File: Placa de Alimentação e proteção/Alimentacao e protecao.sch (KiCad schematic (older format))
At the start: 20 parts, among them J1 PinoCheckBateriaVcc, J2 PinoCheckBateriaGND, J3 8.4V_PlacaCentral, J4 GND_PlacaCentral, Q1 BC548, Q2 BC548, SW1 SW_ON/OFF

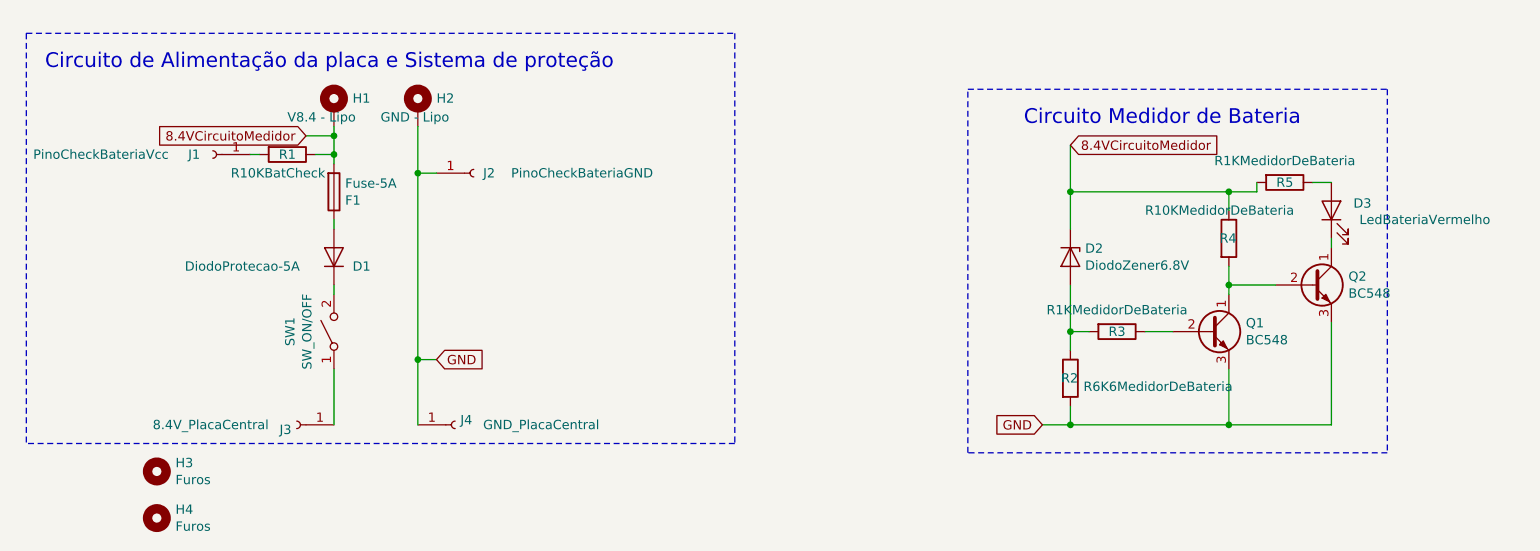
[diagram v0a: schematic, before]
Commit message: Acertos finais para documentação
Foram organizados e preparados para serem folhas em baixo de um um folha hierárquica maior, os projetos das placa de alimentação e das placas de encoder.
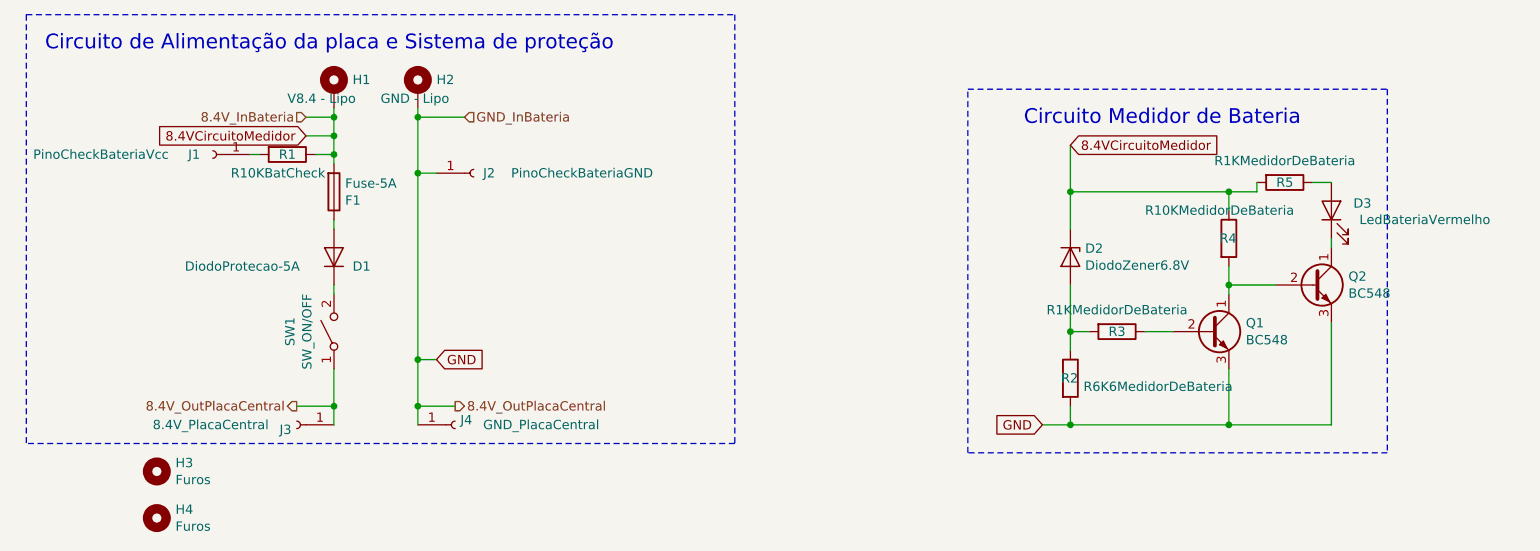
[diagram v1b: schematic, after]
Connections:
- net GND: now also J3.1 (Pin_1), SW1.1 (A)
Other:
- moved on the sheet: H1, H2
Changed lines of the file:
@@
 EESchema Schematic File Version 4
-LIBS:Alimentacao e protecao-cache
-EELAYER 29 0
+EELAYER 30 0
 EELAYER END
 $Descr A4 11693 8268
@@
 L Mechanical:MountingHole_Pad H1
 U 1 1 5D0BE091
-P 2850 1700
-F 0 "H1" H 2950 1751 50  0000 L CNN
-F 1 "V8.4 - Lipo" H 2600 1650 50  0000 L CNN
-F 2 "Connector_Wire:SolderWirePad_1x01_Drill1.5mm" H 2850 1700 50  0001 C CNN
-F 3 "~" H 2850 1700 50  0001 C CNN
-	1    2850 1700
+P 2850 1600
+F 0 "H1" H 2950 1651 50  0000 L CNN
+F 1 "V8.4 - Lipo" H 2600 1550 50  0000 L CNN
+F 2 "Connector_Wire:SolderWirePad_1x01_Drill1.5mm" H 2850 1600 50  0001 C CNN
+F 3 "~" H 2850 1600 50  0001 C CNN
+	1    2850 1600
 	1    0    0    -1
 $EndComp
@@
 L Mechanical:MountingHole_Pad H2
 U 1 1 5D0BE14B
-P 3300 1700
-F 0 "H2" H 3400 1751 50  0000 L CNN
-F 1 "GND - Lipo" H 3100 1650 50  0000 L CNN
-F 2 "Connector_Wire:SolderWirePad_1x01_Drill1.5mm" H 3300 1700 50  0001 C CNN
-F 3 "~" H 3300 1700 50  0001 C CNN
-	1    3300 1700
+P 3300 1600
+F 0 "H2" H 3400 1651 50  0000 L CNN
+F 1 "GND - Lipo" H 3100 1550 50  0000 L CNN
+F 2 "Connector_Wire:SolderWirePad_1x01_Drill1.5mm" H 3300 1600 50  0001 C CNN
+F 3 "~" H 3300 1600 50  0001 C CNN
+	1    3300 1600
 	1    0    0    -1
 $EndComp
@@
 	3400 2050 3300 2050
 Connection ~ 3300 2050
-Wire Wire Line
-	3300 2050 3300 1800
-Text Notes 1300 1500 0    79   ~ 0
+Text Notes 1300 1400 0    79   ~ 0
 Circuito de Alimentação da placa e Sistema de proteção
 Wire Notes Line
-	1200 1300 5000 1300
+	1200 1200 5000 1200
 Wire Notes Line
 	5000 3500 1200 3500
@@
 	2750 1950 2850 1950
 Wire Wire Line
-	2850 1800 2850 1850
-Wire Wire Line
 	2850 1950 2850 2000
 Connection ~ 2850 1950
@@
 Wire Wire Line
 	6800 1900 6800 2150
-Wire Notes Line
-	5000 1300 5000 3500
-Wire Notes Line
-	1200 1300 1200 3500
-Wire Wire Line
-	2850 3100 2850 3400
-Wire Wire Line
-	3300 3400 3300 3050
+Wire Wire Line
+	2850 3100 2850 3300
+Wire Wire Line
+	3300 3400 3300 3300
 Connection ~ 3300 3050
 Wire Wire Line
@@
 	6650 3400 6800 3400
 Connection ~ 6800 3400
+Text HLabel 2650 3300 0    50   Output ~ 0
+8.4V_OutPlacaCentral
+Text HLabel 3500 3300 2    50   Output ~ 0
+8.4V_OutPlacaCentral
+Text HLabel 2700 1750 0    50   Input ~ 0
+8.4V_InBateria
+Text HLabel 3550 1750 2    50   Input ~ 0
+GND_InBateria
+Wire Notes Line
+	1200 1200 1200 3500
+Wire Notes Line
+	5000 1200 5000 3500
+Wire Wire Line
+	2700 1750 2850 1750
+Wire Wire Line
+	2850 1750 2850 1700
+Wire Wire Line
+	2850 1750 2850 1850
+Connection ~ 2850 1750
+Wire Wire Line
+	3300 1700 3300 1750
+Wire Wire Line
+	3300 1750 3550 1750
+Connection ~ 3300 1750
+Wire Wire Line
+	3300 1750 3300 2050
+Wire Wire Line
+	2650 3300 2850 3300
+Connection ~ 2850 3300
+Wire Wire Line
+	2850 3300 2850 3400
+Wire Wire Line
+	3500 3300 3300 3300
+Connection ~ 3300 3300
+Wire Wire Line
+	3300 3300 3300 3050
 $EndSCHEMATC

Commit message: Ajuste final
Acertado a placa central, verificado conflitos de etiquetas hierárquicas, ligados os projeto um no outro, ajustado o projeto principal e linkado todos as placas ao projeto principal.
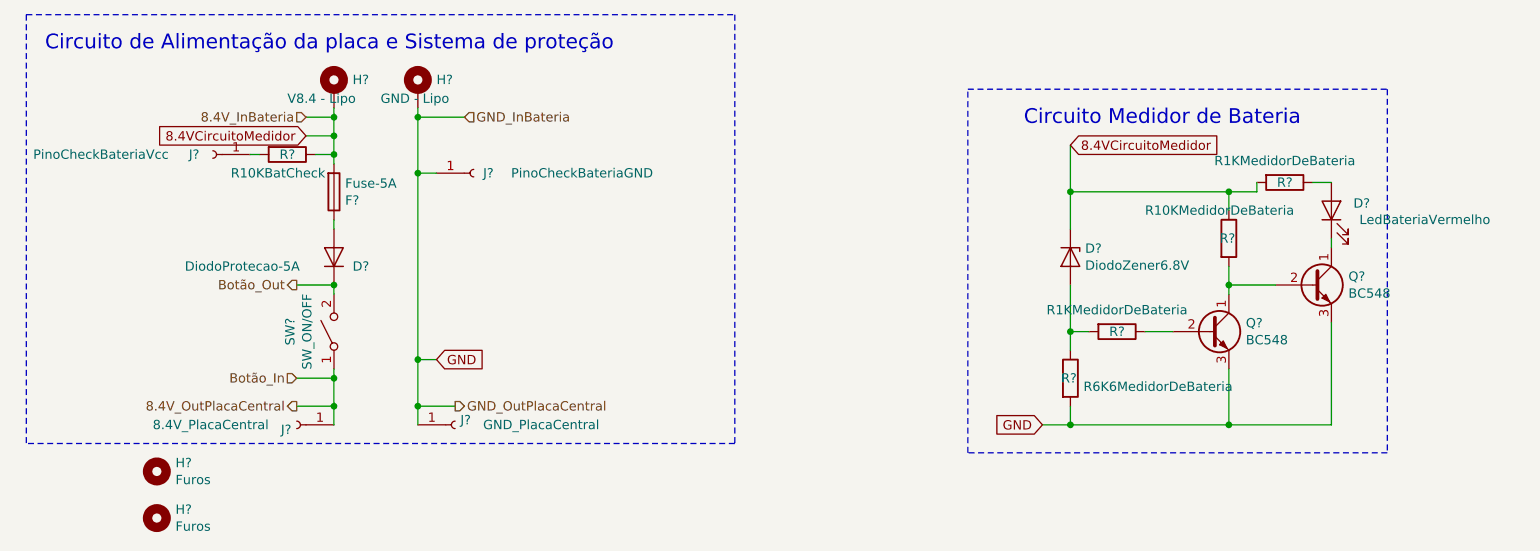
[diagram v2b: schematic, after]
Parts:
- renumbered D1 to D?, D2 to D?, D3 to D?, F1 to F?, H1 to H?, H2 to H?, H3 to H?, H4 to H?, J2 to J?, J1 to J?, J3 to J?, J4 to J?, Q1 to Q?, Q2 to Q?, R1 to R?, R3 to R?, R2 to R?, R4 to R?, R5 to R?, SW1 to SW?
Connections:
- net GND: no longer J?.1 (Pin_1), SW?.1 (A)
- net Botão_Out: now reaches D?.1 (K), SW?.2 (B)
- new net 8.4V_OutPlacaCentral: J?.1 (Pin_1), SW?.1 (A)
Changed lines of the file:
@@
 $Descr A4 11693 8268
 encoding utf-8
-Sheet 1 1
+Sheet 2 7
 Title ""
 Date ""
@@
 $EndDescr
 $Comp
-L Switch:SW_SPST SW1
+L Switch:SW_SPST SW?
 U 1 1 5D0BCA30
 P 2850 2900
-F 0 "SW1" H 2850 3135 50  0000 C CNN
+F 0 "SW?" H 2850 3135 50  0000 C CNN
 F 1 "SW_ON/OFF" H 2850 3044 50  0000 C CNN
 F 2 "CUSTOM_Placa_central_v01:Solder_Pad_Custom" H 2850 2900 50  0001 C CNN
@@
 $EndComp
 $Comp
-L Mechanical:MountingHole_Pad H1
+L Mechanical:MountingHole_Pad H?
 U 1 1 5D0BE091
 P 2850 1600
-F 0 "H1" H 2950 1651 50  0000 L CNN
+F 0 "H?" H 2950 1651 50  0000 L CNN
 F 1 "V8.4 - Lipo" H 2600 1550 50  0000 L CNN
 F 2 "Connector_Wire:SolderWirePad_1x01_Drill1.5mm" H 2850 1600 50  0001 C CNN
@@
 $EndComp
 $Comp
-L Mechanical:MountingHole_Pad H2
+L Mechanical:MountingHole_Pad H?
 U 1 1 5D0BE14B
 P 3300 1600
-F 0 "H2" H 3400 1651 50  0000 L CNN
+F 0 "H?" H 3400 1651 50  0000 L CNN
 F 1 "GND - Lipo" H 3100 1550 50  0000 L CNN
 F 2 "Connector_Wire:SolderWirePad_1x01_Drill1.5mm" H 3300 1600 50  0001 C CNN
@@
 $EndComp
 $Comp
-L Connector:Conn_01x01_Female J2
+L Connector:Conn_01x01_Female J?
 U 1 1 5D152CB0
 P 3600 2050
-F 0 "J2" H 3650 2050 50  0000 L CNN
+F 0 "J?" H 3650 2050 50  0000 L CNN
 F 1 "PinoCheckBateriaGND" H 3800 2050 50  0000 L CNN
 F 2 "Connector_Wire:SolderWirePad_1x01_Drill1.5mm" H 3600 2050 50  0001 C CNN
@@
 $EndComp
 $Comp
-L Device:D D1
+L Device:D D?
 U 1 1 5D153AA9
 P 2850 2500
-F 0 "D1" V 2800 2400 50  0000 R CNN
+F 0 "D?" V 2800 2400 50  0000 R CNN
 F 1 "DiodoProtecao-5A" V 2800 3300 50  0000 R CNN
 F 2 "Diode_THT:D_DO-27_P15.24mm_Horizontal" H 2850 2500 50  0001 C CNN
@@
 $EndComp
 $Comp
-L Device:Fuse F1
+L Device:Fuse F?
 U 1 1 5D154189
 P 2850 2150
-F 0 "F1" H 2910 2196 50  0000 L CNN
+F 0 "F?" H 2910 2196 50  0000 L CNN
 F 1 "Fuse-5A" H 2910 2105 50  0000 L CNN
 F 2 "Fuse:Fuseholder_Cylinder-5x20mm_Stelvio-Kontek_PTF78_Horizontal_Open" V 2780 2150 50  0001 C CNN
@@
 	2850 2650 2850 2700
 $Comp
-L Device:D_Zener D2
+L Device:D_Zener D?
 U 1 1 5D316091
 P 6800 2500
-F 0 "D2" V 6754 2579 50  0000 L CNN
+F 0 "D?" V 6754 2579 50  0000 L CNN
 F 1 "DiodoZener6.8V" V 6845 2579 50  0000 L CNN
 F 2 "Diode_THT:D_DO-35_SOD27_P10.16mm_Horizontal" H 6800 2500 50  0001 C CNN
@@
 $EndComp
 $Comp
-L Device:R R3
+L Device:R R?
 U 1 1 5D316319
 P 7050 2900
-F 0 "R3" V 7050 2900 50  0000 C CNN
+F 0 "R?" V 7050 2900 50  0000 C CNN
 F 1 "R1KMedidorDeBateria" V 6934 2900 50  0000 C CNN
 F 2 "Resistor_THT:R_Axial_DIN0207_L6.3mm_D2.5mm_P10.16mm_Horizontal" V 6980 2900 50  0001 C CNN
@@
 $EndComp
 $Comp
-L Device:R R2
+L Device:R R?
 U 1 1 5D316455
 P 6800 3150
-F 0 "R2" H 6750 3150 50  0000 L CNN
+F 0 "R?" H 6750 3150 50  0000 L CNN
 F 1 "R6K6MedidorDeBateria" H 6870 3105 50  0000 L CNN
 F 2 "Resistor_THT:R_Axial_DIN0207_L6.3mm_D2.5mm_P10.16mm_Horizontal" V 6730 3150 50  0001 C CNN
@@
 $EndComp
 $Comp
-L Transistor_BJT:BC548 Q1
+L Transistor_BJT:BC548 Q?
 U 1 1 5D3166B6
 P 7550 2900
-F 0 "Q1" H 7741 2946 50  0000 L CNN
+F 0 "Q?" H 7741 2946 50  0000 L CNN
 F 1 "BC548" H 7741 2855 50  0000 L CNN
 F 2 "Package_TO_SOT_THT:TO-92_Wide" H 7750 2825 50  0001 L CIN
@@
 $EndComp
 $Comp
-L Device:R R4
+L Device:R R?
 U 1 1 5D316CF8
 P 7650 2400
-F 0 "R4" H 7600 2400 50  0000 L CNN
+F 0 "R?" H 7600 2400 50  0000 L CNN
 F 1 "R10KMedidorDeBateria" H 7200 2550 50  0000 L CNN
 F 2 "Resistor_THT:R_Axial_DIN0207_L6.3mm_D2.5mm_P10.16mm_Horizontal" V 7580 2400 50  0001 C CNN
@@
 $EndComp
 $Comp
-L Device:R R5
+L Device:R R?
 U 1 1 5D31721A
 P 7950 2100
-F 0 "R5" V 7950 2100 50  0000 C CNN
+F 0 "R?" V 7950 2100 50  0000 C CNN
 F 1 "R1KMedidorDeBateria" V 7834 2100 50  0000 C CNN
 F 2 "Resistor_THT:R_Axial_DIN0207_L6.3mm_D2.5mm_P10.16mm_Horizontal" V 7880 2100 50  0001 C CNN
@@
 $EndComp
 $Comp
-L Transistor_BJT:BC548 Q2
+L Transistor_BJT:BC548 Q?
 U 1 1 5D3176BA
 P 8100 2650
-F 0 "Q2" H 8291 2696 50  0000 L CNN
+F 0 "Q?" H 8291 2696 50  0000 L CNN
 F 1 "BC548" H 8291 2605 50  0000 L CNN
 F 2 "Package_TO_SOT_THT:TO-92_Wide" H 8300 2575 50  0001 L CIN
@@
 $EndComp
 $Comp
-L Device:LED D3
+L Device:LED D?
 U 1 1 5D31810C
 P 8200 2250
-F 0 "D3" V 8238 2132 50  0000 R CNN
+F 0 "D?" V 8238 2132 50  0000 R CNN
 F 1 "LedBateriaVermelho" V 8150 2100 50  0000 R CNN
 F 2 "LED_THT:LED_D3.0mm" H 8200 2250 50  0001 C CNN
@@
 	3300 2050 3300 3050
 $Comp
-L Connector:Conn_01x01_Female J3
+L Connector:Conn_01x01_Female J?
 U 1 1 5D3D07BC
 P 2650 3400
-F 0 "J3" H 2678 3426 50  0000 L CNN
+F 0 "J?" H 2678 3426 50  0000 L CNN
 F 1 "8.4V_PlacaCentral" H 2800 3400 50  0000 L CNN
 F 2 "Connector_Wire:SolderWirePad_1x01_Drill1.2mm" H 2650 3400 50  0001 C CNN
@@
 $EndComp
 $Comp
-L Connector:Conn_01x01_Female J4
+L Connector:Conn_01x01_Female J?
 U 1 1 5D3D515E
 P 3500 3400
-F 0 "J4" H 3528 3426 50  0000 L CNN
+F 0 "J?" H 3528 3426 50  0000 L CNN
 F 1 "GND_PlacaCentral" H 3650 3400 50  0000 L CNN
 F 2 "Connector_Wire:SolderWirePad_1x01_Drill1.2mm" H 3500 3400 50  0001 C CNN
@@
 GND
 $Comp
-L Mechanical:MountingHole H3
+L Mechanical:MountingHole H?
 U 1 1 5D58B29C
 P 1900 3650
-F 0 "H3" H 2000 3696 50  0000 L CNN
+F 0 "H?" H 2000 3696 50  0000 L CNN
 F 1 "Furos" H 2000 3605 50  0000 L CNN
 F 2 "Wire_Pads:SolderWirePad_single_2-5mmDrill" H 1900 3650 50  0001 C CNN
@@
 $EndComp
 $Comp
-L Mechanical:MountingHole H4
+L Mechanical:MountingHole H?
 U 1 1 5D58BCCF
 P 1900 3900
-F 0 "H4" H 2000 3946 50  0000 L CNN
+F 0 "H?" H 2000 3946 50  0000 L CNN
 F 1 "Furos" H 2000 3855 50  0000 L CNN
 F 2 "Wire_Pads:SolderWirePad_single_2-5mmDrill" H 1900 3900 50  0001 C CNN
@@
 $EndComp
 $Comp
-L Connector:Conn_01x01_Female J1
+L Connector:Conn_01x01_Female J?
 U 1 1 5D20493D
 P 2200 1950
-F 0 "J1" H 2300 1950 50  0000 C CNN
+F 0 "J?" H 2300 1950 50  0000 C CNN
 F 1 "PinoCheckBateriaVcc" H 2800 1950 50  0000 C CNN
 F 2 "Connector_PinSocket_2.54mm:PinSocket_1x01_P2.54mm_Vertical" H 2200 1950 50  0001 C CNN
@@
 	2400 1950 2450 1950
 $Comp
-L Device:R R1
+L Device:R R?
 U 1 1 5D1A4675
 P 2600 1950
-F 0 "R1" V 2600 1950 50  0000 C CNN
+F 0 "R?" V 2600 1950 50  0000 C CNN
 F 1 "R10KBatCheck" V 2700 1900 50  0000 C CNN
 F 2 "Resistor_THT:R_Axial_DIN0207_L6.3mm_D2.5mm_P10.16mm_Horizontal" V 2530 1950 50  0001 C CNN
@@
 	6800 1900 6800 2150
 Wire Wire Line
-	2850 3100 2850 3300
+	2850 3100 2850 3150
 Wire Wire Line
 	3300 3400 3300 3300
@@
 8.4V_OutPlacaCentral
 Text HLabel 3500 3300 2    50   Output ~ 0
-8.4V_OutPlacaCentral
+GND_OutPlacaCentral
 Text HLabel 2700 1750 0    50   Input ~ 0
 8.4V_InBateria
@@
 Wire Wire Line
 	3300 3300 3300 3050
+Text HLabel 2650 2650 0    50   Output ~ 0
+Botão_Out
+Text HLabel 2650 3150 0    50   Input ~ 0
+Botão_In
+Wire Wire Line
+	2650 2650 2850 2650
+Connection ~ 2850 2650
+Wire Wire Line
+	2650 3150 2850 3150
+Connection ~ 2850 3150
+Wire Wire Line
+	2850 3150 2850 3300
 $EndSCHEMATC
